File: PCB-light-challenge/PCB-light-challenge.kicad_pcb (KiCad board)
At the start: 4 copper layers, 79.9 x 79 mm, 27 parts, among them J1 Conn_01x16_Socket, J3 Conn_01x13_Socket, U2 AP9101CK, U3 SP8K32FRATB

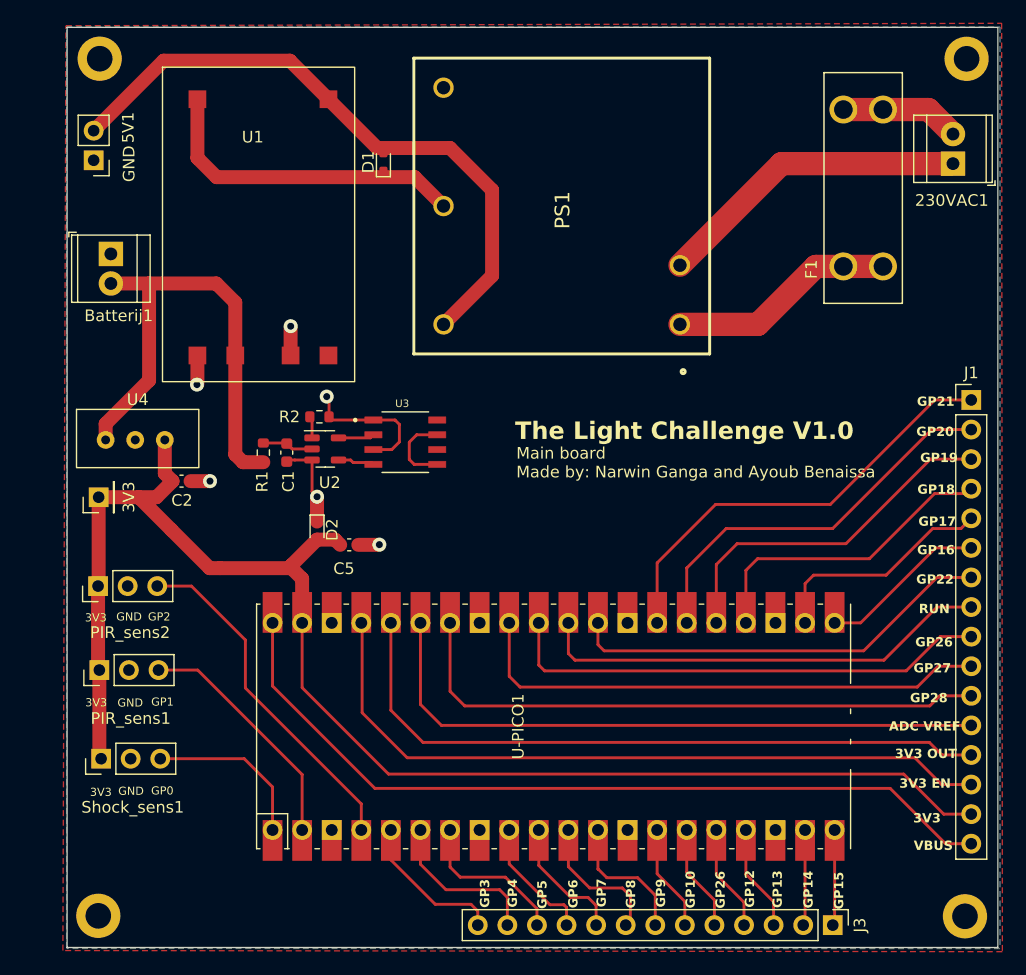
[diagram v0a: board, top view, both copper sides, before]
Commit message: gerber files gemaakt en vias geplaatst  in de main pcb
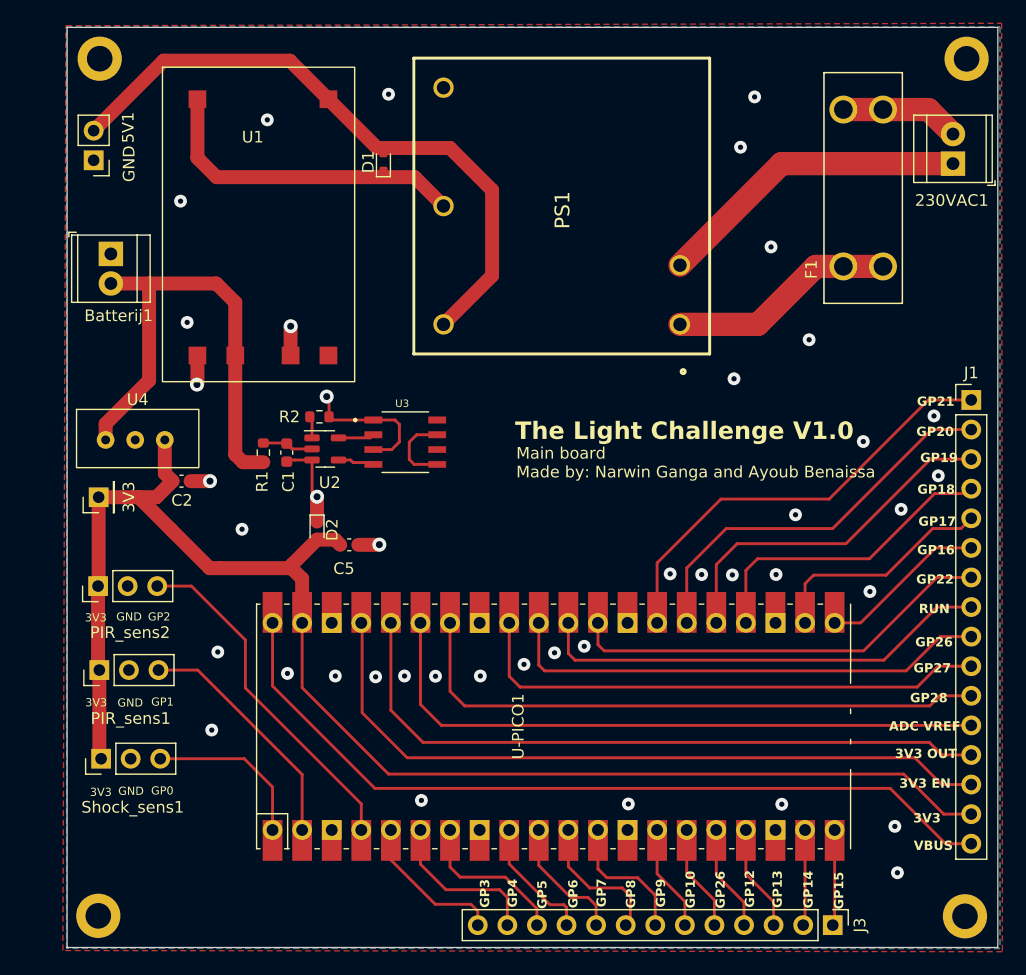
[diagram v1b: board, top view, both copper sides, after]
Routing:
- net GND: vias 6 -> 42
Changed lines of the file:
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@@
       (outputformat 1)
       (mirror false)
-      (drillshape 1)
+      (drillshape 0)
       (scaleselection 1)
-      (outputdirectory "")
+      (outputdirectory "Gerber main pcb/")
     )
   )
@@
   (segment (start 218.02 126.14) (end 218.02 124.27) (width 0.25) (layer "F.Cu") (net 13))
   (segment (start 218.55 126.67) (end 218.02 126.14) (width 0.25) (layer "F.Cu") (net 13))
-  (segment (start 237.97 114.1) (end 228.12 114.1) (width 0.25) (layer "F.Cu") (net 14))
-  (segment (start 250.07 105.13) (end 246.94 105.13) (width 0.25) (layer "F.Cu") (net 14))
   (segment (start 223.1 119.12) (end 223.1 124.27) (width 0.25) (layer "F.Cu") (net 14))
-  (segment (start 246.94 105.13) (end 237.97 114.1) (width 0.25) (layer "F.Cu") (net 14))
-  (segment (start 228.12 114.1) (end 223.1 119.12) (width 0.25) (layer "F.Cu") (net 14))
+  (segment (start 250.07 105.13) (end 246.38 105.13) (width 0.25) (layer "F.Cu") (net 14))
+  (segment (start 228.58 113.64) (end 223.1 119.12) (width 0.25) (layer "F.Cu") (net 14))
+  (segment (start 246.38 105.13) (end 237.87 113.64) (width 0.25) (layer "F.Cu") (net 14))
+  (segment (start 237.87 113.64) (end 228.58 113.64) (width 0.25) (layer "F.Cu") (net 14))
   (segment (start 225.64 119.56) (end 225.64 124.27) (width 0.25) (layer "F.Cu") (net 15))
   (segment (start 250.07 107.67) (end 246.67 107.67) (width 0.25) (layer "F.Cu") (net 15))
@@
   (segment (start 193.9 113.44) (end 193.9 115.57) (width 1.2) (layer "F.Cu") (net 41))
   (segment (start 191.63 98.81) (end 191.64 98.8) (width 0.25) (layer "F.Cu") (net 41))
+  (via (at 182.18 88.06) (size 1.1) (drill 0.45) (layers "F.Cu" "B.Cu") (free) (net 41))
+  (via (at 216.84 126.28) (size 1.1) (drill 0.45) (layers "F.Cu" "B.Cu") (free) (net 41))
+  (via (at 234.98 114.99) (size 1.1) (drill 0.45) (layers "F.Cu" "B.Cu") (free) (net 41))
   (via (at 194.73 104.84) (size 1.2) (drill 0.6) (layers "F.Cu" "B.Cu") (net 41))
+  (via (at 243.51 141.74) (size 1.1) (drill 0.45) (layers "F.Cu" "B.Cu") (free) (net 41))
+  (via (at 232.88 91.99) (size 1.1) (drill 0.45) (layers "F.Cu" "B.Cu") (free) (net 41))
+  (via (at 202.86 139.51) (size 1.1) (drill 0.45) (layers "F.Cu" "B.Cu") (free) (net 41))
+  (via (at 243.73 145.72) (size 1.1) (drill 0.45) (layers "F.Cu" "B.Cu") (free) (net 41))
+  (via (at 201.41 128.83) (size 1.1) (drill 0.45) (layers "F.Cu" "B.Cu") (free) (net 41))
+  (via (at 224.22 120.06) (size 1.1) (drill 0.45) (layers "F.Cu" "B.Cu") (free) (net 41))
+  (via (at 231.47 79.11) (size 1.1) (drill 0.45) (layers "F.Cu" "B.Cu") (free) (net 41))
   (via (at 199.25 117.55) (size 1.2) (drill 0.6) (layers "F.Cu" "B.Cu") (net 41))
+  (via (at 198.93 128.9) (size 1.1) (drill 0.45) (layers "F.Cu" "B.Cu") (free) (net 41))
   (via (at 193.9 113.44) (size 1.2) (drill 0.6) (layers "F.Cu" "B.Cu") (net 41))
+  (via (at 246.87 106.5) (size 1.1) (drill 0.45) (layers "F.Cu" "B.Cu") (free) (net 41))
+  (via (at 220.63 139.82) (size 1.1) (drill 0.45) (layers "F.Cu" "B.Cu") (free) (net 41))
+  (via (at 184.86 133.47) (size 1.1) (drill 0.45) (layers "F.Cu" "B.Cu") (free) (net 41))
+  (via (at 189.63 81.08) (size 1.1) (drill 0.45) (layers "F.Cu" "B.Cu") (free) (net 41))
+  (via (at 247.24 111.64) (size 1.1) (drill 0.45) (layers "F.Cu" "B.Cu") (free) (net 41))
+  (via (at 187.46 116.23) (size 1.1) (drill 0.45) (layers "F.Cu" "B.Cu") (free) (net 41))
+  (via (at 211.67 127.83) (size 1.1) (drill 0.45) (layers "F.Cu" "B.Cu") (free) (net 41))
+  (via (at 229.56 120.15) (size 1.1) (drill 0.45) (layers "F.Cu" "B.Cu") (free) (net 41))
+  (via (at 204.07 128.85) (size 1.1) (drill 0.45) (layers "F.Cu" "B.Cu") (free) (net 41))
+  (via (at 241.37 121.58) (size 1.1) (drill 0.45) (layers "F.Cu" "B.Cu") (free) (net 41))
+  (via (at 191.36 128.61) (size 1.1) (drill 0.45) (layers "F.Cu" "B.Cu") (free) (net 41))
+  (via (at 200.04 78.88) (size 1.1) (drill 0.45) (layers "F.Cu" "B.Cu") (free) (net 41))
+  (via (at 233.8 139.84) (size 1.1) (drill 0.45) (layers "F.Cu" "B.Cu") (free) (net 41))
+  (via (at 244.05 114.52) (size 1.1) (drill 0.45) (layers "F.Cu" "B.Cu") (free) (net 41))
   (via (at 191.64 98.8) (size 1.2) (drill 0.6) (layers "F.Cu" "B.Cu") (net 41))
+  (via (at 195.47 128.83) (size 1.1) (drill 0.45) (layers "F.Cu" "B.Cu") (free) (net 41))
+  (via (at 185.38 126.77) (size 1.1) (drill 0.45) (layers "F.Cu" "B.Cu") (free) (net 41))
+  (via (at 229.7 103.31) (size 1.1) (drill 0.45) (layers "F.Cu" "B.Cu") (free) (net 41))
+  (via (at 236.15 99.96) (size 1.1) (drill 0.45) (layers "F.Cu" "B.Cu") (free) (net 41))
+  (via (at 240.8 108.7) (size 1.1) (drill 0.45) (layers "F.Cu" "B.Cu") (free) (net 41))
+  (via (at 214.29 126.84) (size 1.1) (drill 0.45) (layers "F.Cu" "B.Cu") (free) (net 41))
+  (via (at 207.92 128.83) (size 1.1) (drill 0.45) (layers "F.Cu" "B.Cu") (free) (net 41))
+  (via (at 230.26 83.43) (size 1.1) (drill 0.45) (layers "F.Cu" "B.Cu") (free) (net 41))
   (via (at 184.71 112.1) (size 1.2) (drill 0.6) (layers "F.Cu" "B.Cu") (net 41))
+  (via (at 182.75 98.47) (size 1.1) (drill 0.45) (layers "F.Cu" "B.Cu") (free) (net 41))
   (via (at 183.59 103.81) (size 1.2) (drill 0.6) (layers "F.Cu" "B.Cu") (net 41))
+  (via (at 226.92 120.12) (size 1.1) (drill 0.45) (layers "F.Cu" "B.Cu") (free) (net 41))
+  (via (at 233.31 120.12) (size 1.1) (drill 0.45) (layers "F.Cu" "B.Cu") (free) (net 41))
   (segment (start 183.63 79.31) (end 183.63 84.35) (width 1.2) (layer "F.Cu") (net 42))
   (segment (start 202.28 86) (end 204.76 88.48) (width 1.2) (layer "F.Cu") (net 42))

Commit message: TP footprint verandert,  apparte grond (P-) gemaakt.  AC  clearance verandert.  connector voor PIR verandert
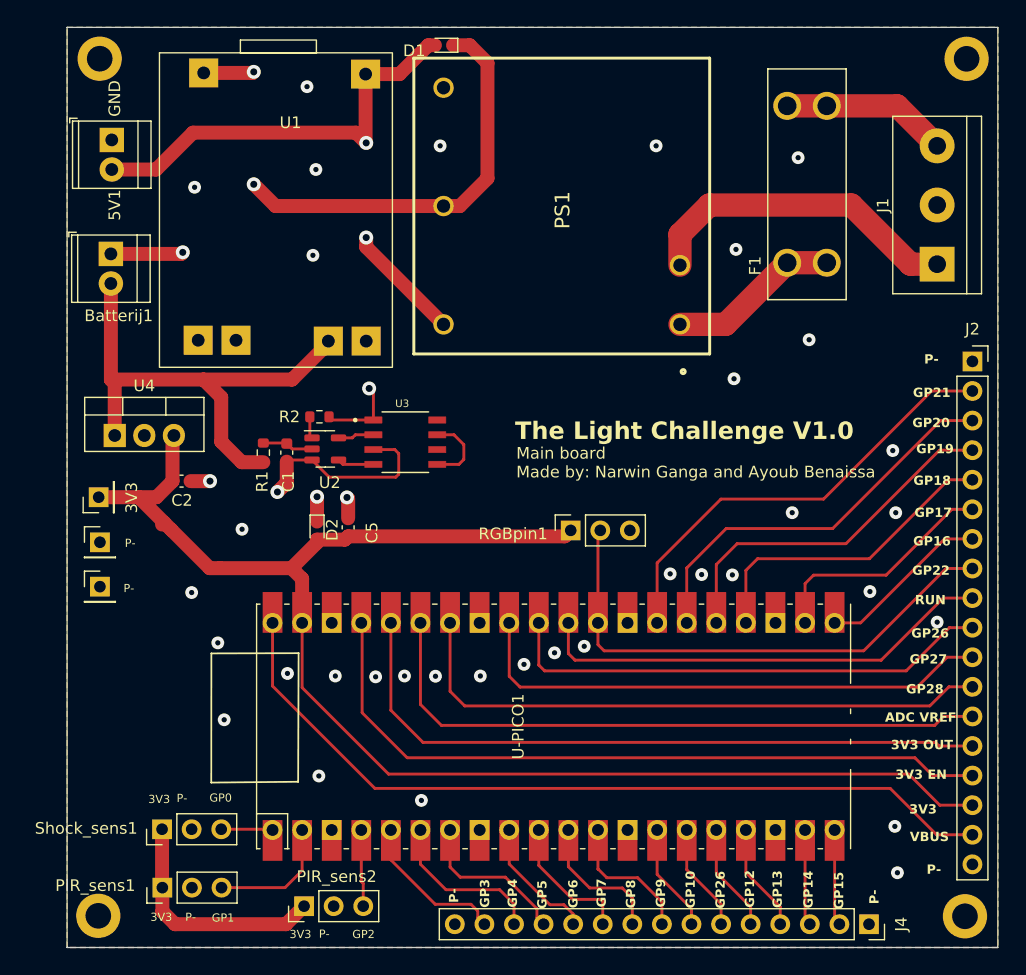
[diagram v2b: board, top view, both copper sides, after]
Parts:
- removed 230VAC1: Screw_Terminal_01x02, TerminalBlock_TE-Connectivity:TerminalBlock_TE_282834-2_1x02_P2.54mm_Horizontal
- removed J3: Conn_01x13_Socket, Connector_PinHeader_2.54mm:PinHeader_1x13_P2.54mm_Vertical
- added J2: Conn_01x18_Socket, Connector_PinSocket_2.54mm:PinSocket_1x18_P2.54mm_Vertical, F.Cu at (250.2, 101.8)
- added J4: Conn_01x15_Socket, Connector_PinSocket_2.54mm:PinSocket_1x15_P2.54mm_Vertical, F.Cu at (241.3, 150.1)
- added P-1: Conn_01x01_Socket, Connector_PinHeader_2.54mm:PinHeader_1x01_P2.54mm_Vertical, F.Cu at (175.3, 117.3)
- added P-2: Conn_01x01_Socket, Connector_PinHeader_2.54mm:PinHeader_1x01_P2.54mm_Vertical, F.Cu at (175.3, 121.2)
- added RGBpin1: Conn_01x03_Socket, Connector_PinSocket_2.54mm:PinSocket_1x03_P2.54mm_Vertical, F.Cu at (215.7, 116.3)
- 5V1: footprint Connector_PinHeader_2.54mm:PinHeader_1x02_P2.54mm_Vertical -> TerminalBlock_TE-Connectivity:TerminalBlock_TE_282834-2_1x02_P2.54mm_Horizontal
- J1: value Conn_01x16_Socket -> Screw_Terminal_01x03; footprint Connector_PinHeader_2.54mm:PinHeader_1x16_P2.54mm_Vertical -> TerminalBlock:TerminalBlock_bornier-3_P5.08mm
- U4: footprint LDO:LDO- TO220FP -> Package_TO_SOT_THT:TO-220-3_Vertical
- moved PIR_sens2 32.7 mm to (192.8, 148.6)
- moved PIR_sens1 19.4 mm to (180.6, 147.0)
- moved J1 12.0 mm to (247.1, 93.5), turned to 90 degrees
- moved D1 11.3 mm to (204.7, 74.7), turned to 180 degrees
- moved U4 8.38 mm to (176.5, 108.2)
- moved Shock_sens1 8.00 mm to (180.6, 142.0)
- moved F1 4.83 mm to (236.0, 86.6)
- moved U1 3.47 mm to (177.1, 78.1)
- moved 5V1 2.34 mm to (176.3, 82.8), turned to -90 degrees
- moved C5 1.51 mm to (196.6, 116.1), turned to 90 degrees
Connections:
- Batterij1 pad 1: GND -> Batterij-
- Batterij1 pad 2: BAT+ -> Batterij+
- C1 pad 2: GND -> Batterij-
- C2 pad 2: GND -> P-
- C5 pad 2: GND -> P-
- D2 pad 1: GND -> P-
- J1 pad 1: GP21 -> /Battery_charger/GNDAC
- J1 pad 2: GP20 -> unconnected-(J1-Pin_2-Pad2)
- J1 pad 3: GP19 -> /Battery_charger/Fuse_in
- PIR_sens1 pad 2: GND -> P-
- PIR_sens2 pad 2: GND -> P-
- R1 pad 1: BAT+ -> Batterij+
- R2 pad 1: GND -> P-
- Shock_sens1 pad 2: GND -> P-
- U-PICO1 pad 13: GND -> P-
- U-PICO1 pad 18: GND -> P-
- U-PICO1 pad 23: GND -> P-
- U-PICO1 pad 28: GND -> P-
- U-PICO1 pad 3: GND -> P-
- U-PICO1 pad 33: GND -> P-
- U-PICO1 pad 38: GND -> P-
- U-PICO1 pad 8: GND -> P-
- U1 pad 3: BAT+ -> P-
- U1 pad 4: GND -> Batterij+
- U2 pad 3: GND -> Batterij-
- U3 pad 1: GND -> P-
- U3 pad 3: GND -> Batterij-
- U4 pad 1: BAT+ -> Batterij+
- U4 pad 2: GND -> P-
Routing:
- net Batterij-: track 0.00 -> 55.1 mm, vias 0 -> 2
- net Batterij+: track 0.00 -> 43.7 mm
- net BAT+: track 42.5 -> 0.00 mm
- net GND: track 28.3 -> 0.00 mm, vias 42 -> 35
- net GP2: track 29.9 -> 6.61 mm
- net Net-(D1-A1): track 27.9 -> 49.3 mm, vias 0 -> 2
- net 3V3: track 127.5 -> 145.3 mm
- net P-: track 0.00 -> 12.4 mm, vias 0 -> 4
- net GP1: track 22.8 -> 11.0 mm
- net GP0: track 14.3 -> 4.43 mm
- net GP22: track 36.7 -> 45.2 mm
- net /Battery_charger/Fuse: track 19.5 -> 14.8 mm
- net /Battery_charger/Fuse_in: track 10.3 -> 14.3 mm
- net /Battery_charger/GNDAC: track 27.1 -> 27.9 mm
- net GP7: track 11.1 -> 11.8 mm
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- added copper zone on In1.Cu, net P-
- removed copper zone on In1.Cu, net GND
- removed copper zone on In2.Cu, net GND
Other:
- board text added: "P-"

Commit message: Vias  kleiner gemaakt en grond GND genoemd op silkscreen
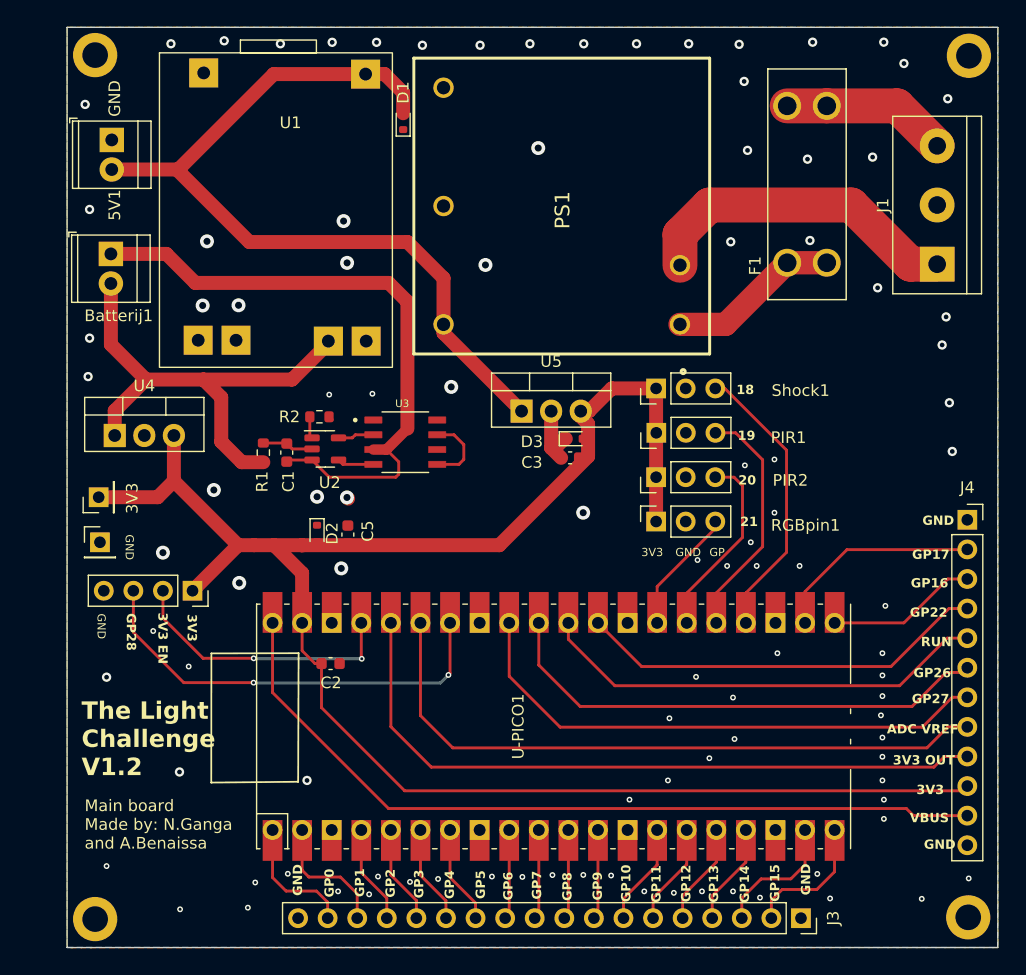
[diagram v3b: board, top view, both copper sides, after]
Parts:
- removed P-2: Conn_01x01_Socket, Connector_PinHeader_2.54mm:PinHeader_1x01_P2.54mm_Vertical
- added C3: 100n, Capacitor_SMD:C_0603_1608Metric, F.Cu at (215.6, 110.1)
- added D3: ESD9B3.3ST5G, Diode_SMD:D_SOD-523, F.Cu at (216.0, 108.5)
- added J3: Conn_01x18_Socket, Connector_PinSocket_2.54mm:PinSocket_1x18_P2.54mm_Vertical, F.Cu at (235.4, 149.6)
- added U5: ~, Package_TO_SOT_THT:TO-220-3_Vertical, F.Cu at (211.5, 106.1)
- H1, H2, H3, H4: value MountingHole_Pad -> MountingHole
- J2: value Conn_01x18_Socket -> Conn_01x04_Socket; footprint Connector_PinSocket_2.54mm:PinSocket_1x18_P2.54mm_Vertical -> Connector_PinSocket_2.54mm:PinSocket_1x04_P2.54mm_Vertical
- J4: value Conn_01x15_Socket -> Conn_01x12_Socket; footprint Connector_PinSocket_2.54mm:PinSocket_1x15_P2.54mm_Vertical -> Connector_PinSocket_2.54mm:PinSocket_1x12_P2.54mm_Vertical
- moved H2 105.1 mm to (174.8, 75.5)
- moved H4 74.7 mm to (249.8, 149.6)
- moved H1 73.9 mm to (174.8, 149.7)
- moved J2 69.8 mm to (183.2, 121.5), turned to -90 degrees
- moved PIR1 57.6 mm to (223.0, 108.0)
- moved Shock1 56.8 mm to (223.0, 104.1)
- moved PIR2 47.6 mm to (223.0, 111.8)
- moved J4 35.7 mm to (249.7, 115.4), turned to 0 degrees
- moved C2 20.2 mm to (195.1, 127.8)
- moved D1 7.38 mm to (201.3, 81.2), turned to 90 degrees
- moved RGBpin1 7.37 mm to (223.0, 115.6)
- moved C5 0.62 mm to (196.5, 116.7)
- moved H3 0.33 mm to (249.9, 75.6)
- moved D2 0.32 mm to (193.9, 116.6)
- renumbered PIR_sens1 to PIR1, PIR_sens2 to PIR2, Shock_sens1 to Shock1
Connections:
- 5V1 pad 1: GND -> P-
- D1 pad 1: Net-(D1-A1) -> P-
- H1 pad 1: GND -> (no net)
- H2 pad 1: GND -> (no net)
- H3 pad 1: GND -> (no net)
- H4 pad 1: GND -> (no net)
- J2 pad 1: P- -> 3V3
- J2 pad 2: GP21 -> 3V3 EN
- J2 pad 3: GP20 -> GP28
- J2 pad 4: GP19 -> P-
- J4 pad 10: GP7 -> 3V3
- J4 pad 11: GP6 -> VBUS
- J4 pad 12: GP5 -> P-
- J4 pad 2: GP15 -> GP17
- J4 pad 3: GP14 -> GP16
- J4 pad 4: GP13 -> GP22
- J4 pad 5: GP12 -> RUN
- J4 pad 6: GP11 -> GP26
- J4 pad 7: GP10 -> GP27
- J4 pad 8: GP9 -> ADC VREF
- J4 pad 9: GP8 -> 3V3 OUT
- PIR1 pad 3: GP1 -> GP19
- PIR2 pad 3: GP2 -> GP20
- PS1 pad 4: Net-(D1-A1) -> P-
- RGBpin1 pad 2: GP22 -> P-
- RGBpin1 pad 3: P- -> GP21
- Shock1 pad 3: GP0 -> GP18
- U1 pad 1: GND -> P-
- U1 pad 5: Net-(D1-A1) -> P-
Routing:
- net Net-(D1-A1): track 49.3 -> 0.00 mm, vias 2 -> 0
- net 3V3 EN: track 62.4 -> 24.1 mm, vias 0 -> 2
- net GP21: track 38.3 -> 10.8 mm
- net GP20: track 34.5 -> 16.4 mm
- net +5V: track 54.8 -> 71.9 mm, vias 2 -> 0
- net GP28: track 51.9 -> 37.2 mm, vias 0 -> 2
- net 3V3: track 145.3 -> 156.2 mm
- net GP19: track 31.1 -> 20.7 mm
- net GP22: track 45.2 -> 35.3 mm
- net GP0: track 4.43 -> 11.1 mm
- net P-: track 12.4 -> 6.48 mm, vias 4 -> 103
- net GP4: track 14.1 -> 8.48 mm
- net GP5: track 13.7 -> 8.48 mm
- net GP3: track 13.2 -> 8.48 mm
- net GP8: track 12.0 -> 7.71 mm
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- added copper zone on B.Cu, net P-
- added copper zone on F.Cu, net P-
- removed copper zone on B.Cu, net GND
- removed copper zone on F.Cu, net GND
- removed copper zone on In1.Cu, net P-
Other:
- copper layers 4 -> 2
- board text added: "18"
- board text added: "19"
- board text added: "20"
- board text added: "21"
- board text added: "GP"
- board text added: "GP11"
- board text added: "Main board Made by: N.Ganga and A.Benaissa"
- board text added: "The Light Challenge V1.2"
- board text removed: "GP18"
- board text removed: "GP19"
- board text removed: "GP20"
- board text removed: "GP21"
- board text removed: "Main board Made by: Narwin Ganga and Ayoub Benaissa"
- board text removed: "P-"
- board text removed: "The Light Challenge V1.0"

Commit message: Extra caps toegevoegd
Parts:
- added C10: C_Polarized, Capacitor_THT:CP_Radial_Tantal_D5.5mm_P2.50mm, F.Cu at (211.2, 111.2)
- added C4: C_Polarized, Capacitor_THT:CP_Radial_Tantal_D5.5mm_P2.50mm, F.Cu at (216.8, 114.4)
- added C6: C_Polarized, Capacitor_THT:CP_Radial_Tantal_D5.5mm_P2.50mm, F.Cu at (181.6, 112.6)
- added C7: 100n, Capacitor_SMD:C_0603_1608Metric, F.Cu at (196.0, 103.4)
- added C8: C_Polarized, Capacitor_THT:CP_Radial_Tantal_D5.5mm_P2.50mm, F.Cu at (177.4, 101.2)
- added C9: 100n, Capacitor_SMD:C_0603_1608Metric, F.Cu at (210.1, 115.3)
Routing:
- net +5V: track 71.9 -> 81.3 mm
- net Batterij+: track 42.9 -> 46.4 mm
- net 3V3: track 156.2 -> 159.1 mm
- net P-: vias 103 -> 98
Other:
- board text added: "+"
- board text added: "-"
- board text added: "Main board Made by: N.Ganga, A.Benaissa, J.Meijer & Y.Kersten"
- board text removed: "Main board Made by: N.Ganga and A.Benaissa"
